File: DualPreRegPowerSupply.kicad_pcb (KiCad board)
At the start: 4 copper layers, 100 x 100 mm, 330 parts, among them J101 Power Input, J102 Conn_01x03_Pin, J103 Conn_02x02_Odd_Even, J201 Banana_Red, J202 Banana_Black, J401 Conn_02x05_Odd_Even, J402 Banana_Red, J403 Banana_Black, J601 Power Input, J801 Conn_01x03_Pin, J802 Conn_02x02_Odd_Even, J901 Power Input, M401 Fan_4pin, Q101 MMBT3906, Q102 BCP56, Q103 BSS138, Q104 TIP125, Q105 BSS138, Q106 BSS138, Q107 BCP56, Q301 BCP56, Q302 BSS138, Q303 TIP125, Q304 BCP56, Q401 BSS138, Q501 MMBT3906, Q801 BSS138, Q802 BSS138, U1002 AP7383, U1003 LM2776, U1004 XC6901D121MR-G, U101 TLV4387PWR, U102 ISO6721RFBD, U104 LT8612, U105 LMV331, U106 ATtiny1614-SS, U107 ADS1118IDGS, U108 MCP48FVB22, U109 AP7383, U110 LM2776, U111 XC6901D121MR-G, U1501 LMR51606, U301 TLV4387PWR, U302 LMV331, U401 TMP1075D, U501 LT8612, U601 LMR51606, U701 ADS1118IDGS, U702 MCP48FVB22, U801 ISO6721RFBD, U802 ATtiny1614-SS, U901 AP63200WU

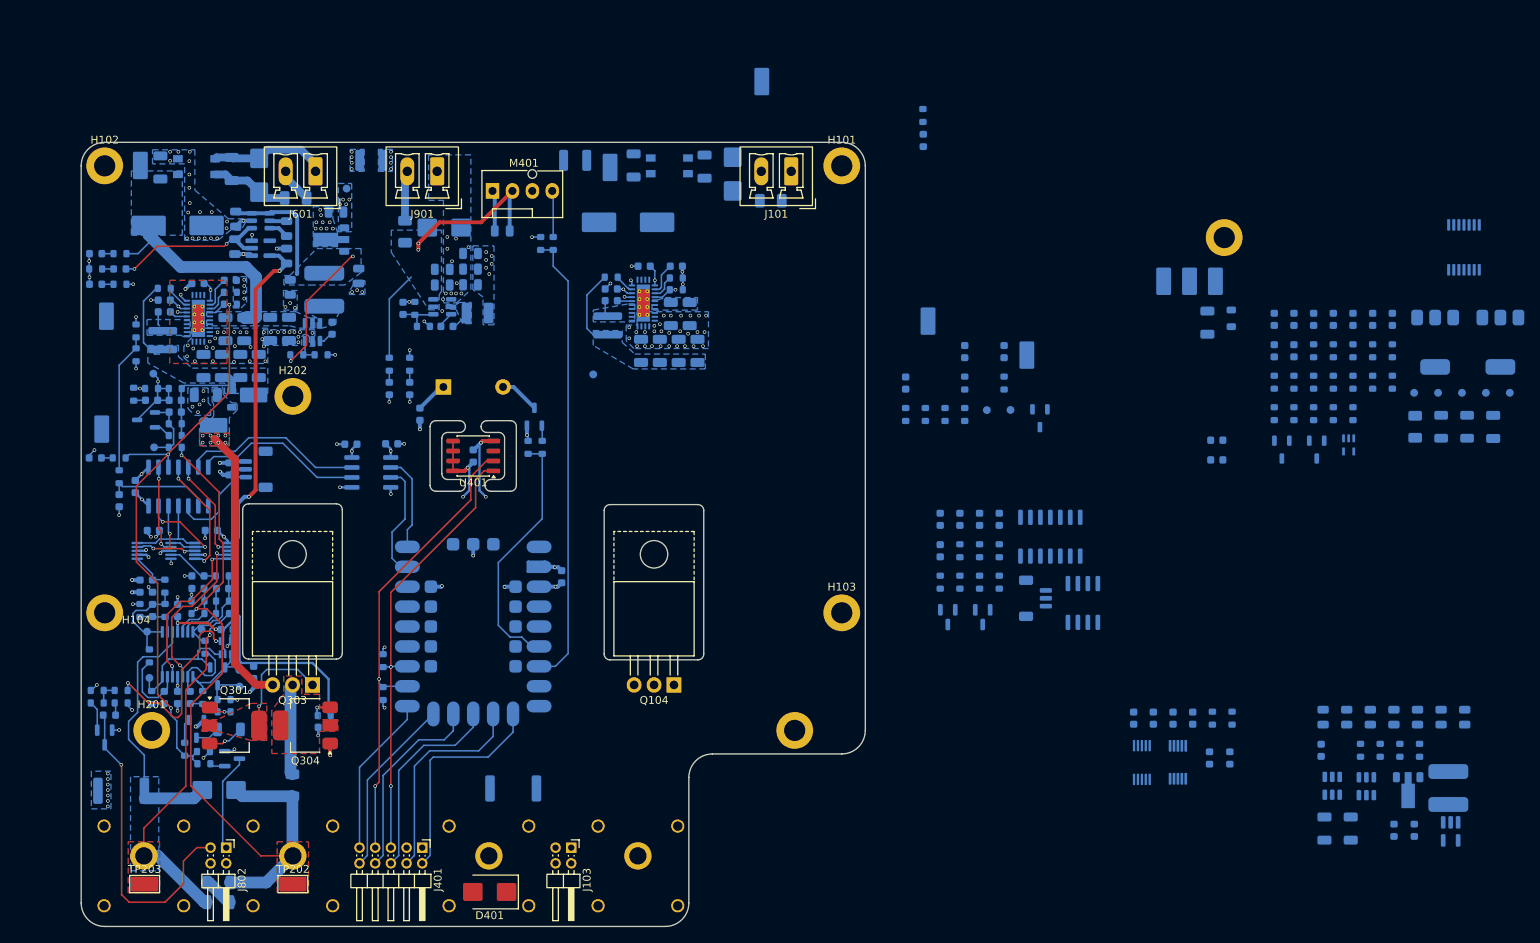
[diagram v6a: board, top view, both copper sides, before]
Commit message: added loop calc
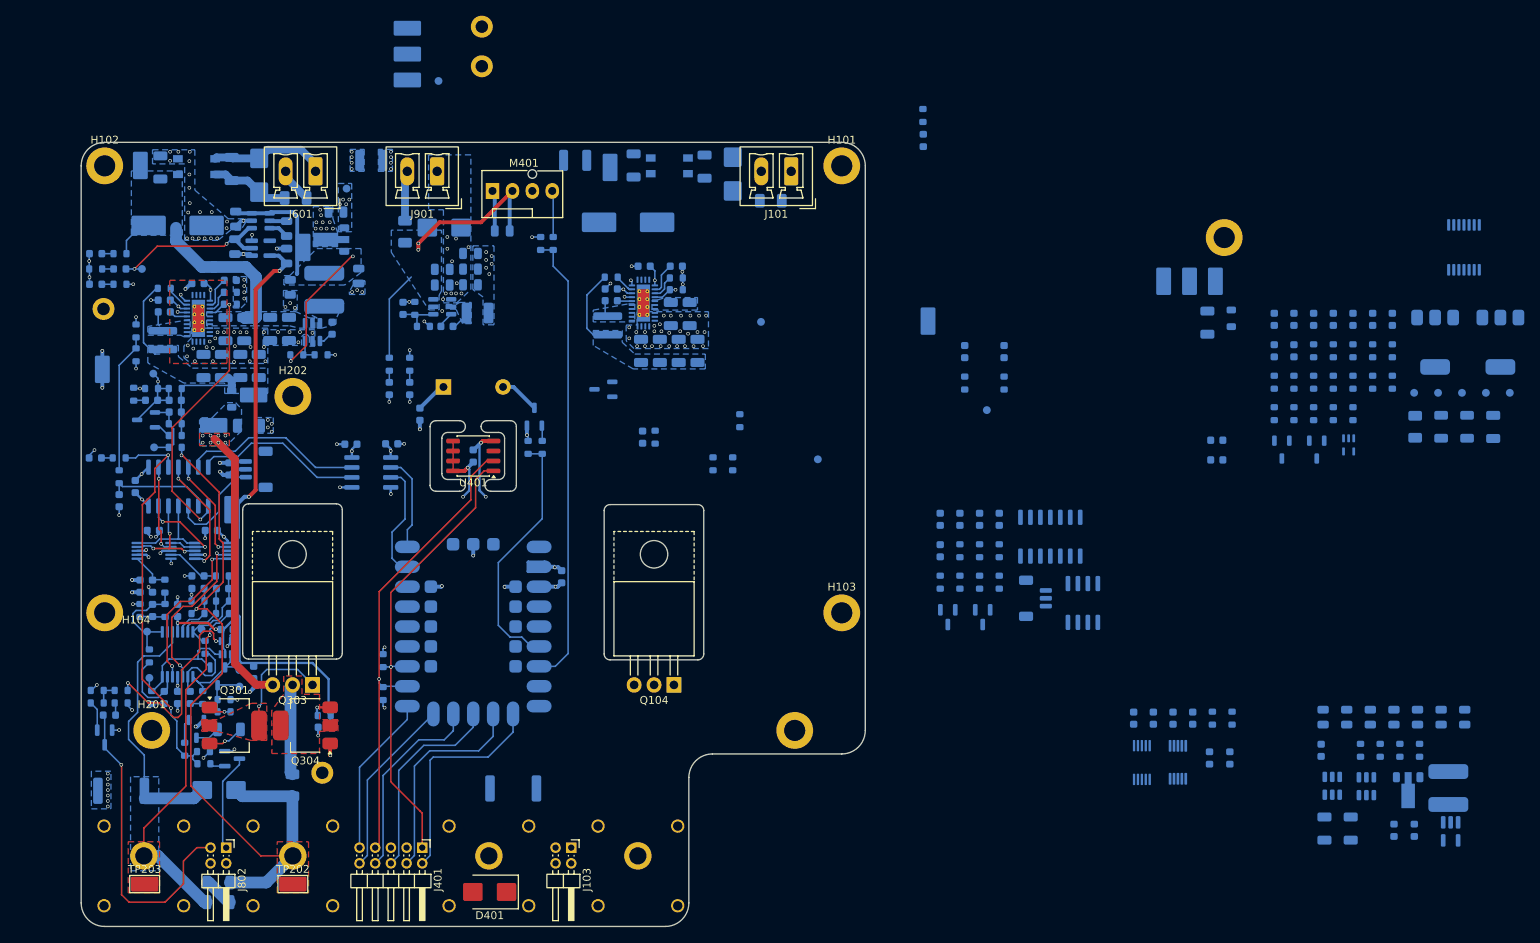
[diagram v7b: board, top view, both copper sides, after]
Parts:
- removed TP109, TP111, TP504, TP602: TestPoint, LibEigen:SMD Test Point PCWCTE
- added TP1501: TestPoint_Alt, TestPoint:TestPoint_Keystone_5005-5009_Compact, B.Cu at (151.1, 36.3)
- added TP1502: TestPoint_Alt, TestPoint:TestPoint_Keystone_5005-5009_Compact, B.Cu at (151.1, 31.2)
- added TP1503: TestPoint, LibEigen:SMD Test Point PCWCTE, B.Cu at (141.6, 38.0)
- added TP1504: TestPoint, LibEigen:SMD Test Point PCWCTE, B.Cu at (141.6, 34.8)
- added TP1505: TestPoint, LibEigen:SMD Test Point PCWCTE, B.Cu at (141.6, 31.4)
- added TP1506: TestPoint_Alt, TestPoint:TestPoint_Pad_D1.0mm, B.Cu at (145.6, 38.2)
- added TP603: TestPoint_Alt, TestPoint:TestPoint_Keystone_5005-5009_Compact, B.Cu at (102.8, 67.2)
- added TP604: TestPoint_Alt, TestPoint:TestPoint_Keystone_5005-5009_Compact, B.Cu at (130.8, 126.4)
- added TP605: TestPoint, LibEigen:SMD Test Point PCWCTE, B.Cu at (128.3, 59.4)
- added TP606: TestPoint, LibEigen:SMD Test Point PCWCTE, B.Cu at (102.7, 75.0)
- added TP607: TestPoint, LibEigen:SMD Test Point PCWCTE, B.Cu at (119.2, 92.8)
- added TP608: TestPoint_Alt, TestPoint:TestPoint_Pad_D1.0mm, B.Cu at (107.8, 62.1)
- moved Q101 55.8 mm to (166.6, 77.5), turned to 180 degrees
- moved R130 37.1 mm to (173.2, 83.6), turned to 90 degrees
- moved C137 34.3 mm to (171.6, 83.6)
- moved R133 28.7 mm to (184.0, 81.5)
- moved TP110 25.4 mm to (193.9, 86.4)
- moved R125 25.4 mm to (180.6, 87.0)
- moved R126 25.4 mm to (183.1, 87.0)
- moved TP106 22.4 mm to (186.7, 68.9)
- moved C201 6.76 mm to (121.4, 82.2), turned to 0 degrees
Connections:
- J401 pad 1: GNDD -> /Control/SDA
- J401 pad 5: /Control/SDA -> GNDD
- R120 pad 2: /Ch1Power1/DCDCTracking/Enable -> /Ch1Power1/Linear_PostReg/OE
- R123 pad 2: /Ch1Power1/DCDCTracking/Enable -> /Ch1Power1/Linear_PostReg/OE
- R124 pad 1: /Ch1Power1/DCDCTracking/Enable -> /Ch1Power1/Linear_PostReg/OE
- R135 pad 1: /Ch1Power1/DCDCTracking/Enable -> /Ch1Power1/Linear_PostReg/OE
- R310 pad 2: /Ch1Power/DCDCTracking/Enable -> /Ch1Power/Linear_PostReg/OE
- R312 pad 2: /Ch1Power/DCDCTracking/Enable -> /Ch1Power/Linear_PostReg/OE
- R803 pad 1: /Ch1Power/DCDCTracking/Enable -> /Ch1Power/Linear_PostReg/OE
- R804 pad 1: /Ch1Power/DCDCTracking/Enable -> /Ch1Power/Linear_PostReg/OE
- U106 pad 3: /Ch1Power1/DCDCTracking/Enable -> /Ch1Power1/Linear_PostReg/OE
- U106 pad 8: unconnected-(U106-PB1-Pad8) -> /Ch1Power1/DCDCTracking/Enable
- U802 pad 3: /Ch1Power/DCDCTracking/Enable -> /Ch1Power/Linear_PostReg/OE
- U802 pad 8: unconnected-(U802-PB1-Pad8) -> /Ch1Power/DCDCTracking/Enable
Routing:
- net /Ch1Power/Linear_PostReg/OE: track 0.00 -> 52.1 mm, vias 0 -> 2
- net /Ch1Power/DCDCTracking/Enable: track 78.2 -> 37.0 mm, vias 3 -> 2
- net +3V3Ch1: track 26.2 -> 30.9 mm, vias 20 -> 22
- net +40VCh1: track 27.9 -> 25.8 mm
- net /Control/SDA: track 57.6 -> 59.2 mm, vias 2 -> 1
- net Net-(D1002-K): track 20.8 -> 21.8 mm
- net /Ch1Power/MCU/UPDI: track 12.1 -> 12.9 mm
- net GND_Ch1: vias 121 -> 115
- net /Control/SCL: vias 2 -> 1
